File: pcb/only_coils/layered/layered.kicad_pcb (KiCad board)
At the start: 4 copper layers, 70 x 50 mm, 8 parts, among them J2 Conn_01x06_Pin, J4 Conn_01x03_Pin

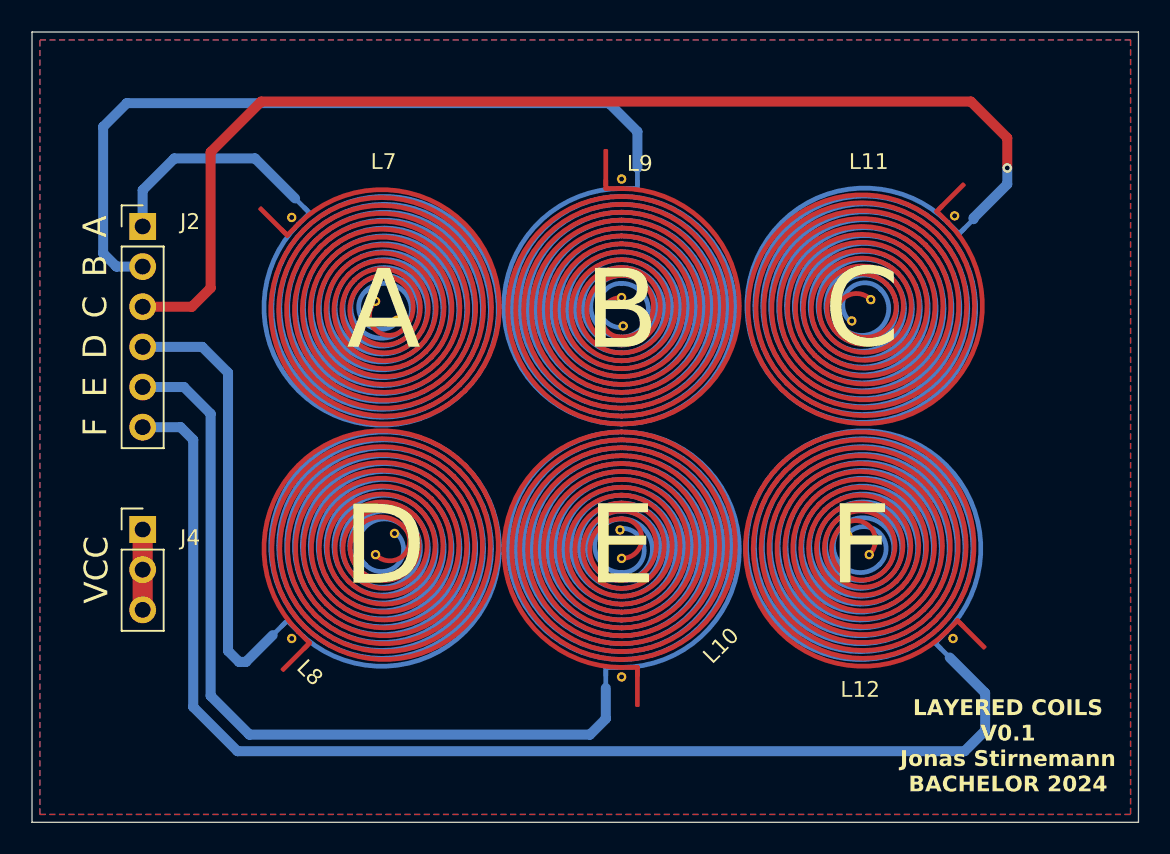
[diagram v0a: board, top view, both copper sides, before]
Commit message: Added small script for square coils
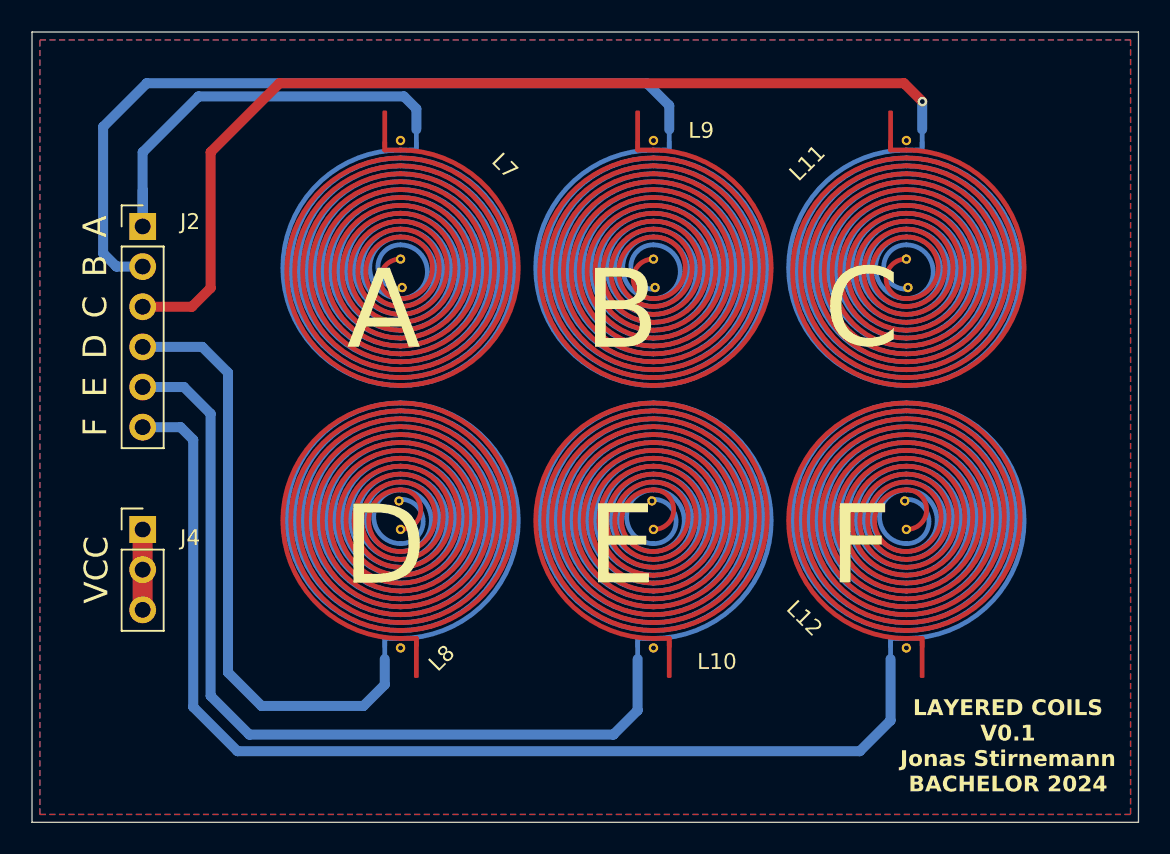
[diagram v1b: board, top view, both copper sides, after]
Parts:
- moved L11 3.66 mm to (122.0, 50.0), turned to 90 degrees
- moved L12 3.44 mm to (122.0, 65.5), turned to -90 degrees
- moved L9 3.16 mm to (106.0, 50.0)
- moved L10 2.73 mm to (106.0, 65.5)
- moved L7 2.64 mm to (90.0, 50.0), turned to 90 degrees
- moved L8 2.10 mm to (90.0, 65.5), turned to -90 degrees
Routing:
- net /A: track 13.8 -> 27.4 mm
- net /D: track 27.5 -> 38.0 mm
- net /C: track 72.1 -> 62.5 mm
- net /F: track 77.8 -> 70.4 mm
- net /E: track 51.2 -> 54.8 mm
- net /B: track 48.3 -> 49.9 mm
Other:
- board text added: "LAYERED MODULE - 4 layer coils - 12 turns / layer - 0.3 mm traces - 0.2 mm gap"
- board text removed: "LAYERED MODULE - 4 layer coils - 12 turns / layer - 0.3 mils traces - 0.2 mils gap"

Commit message: Added finished linear coils PCB
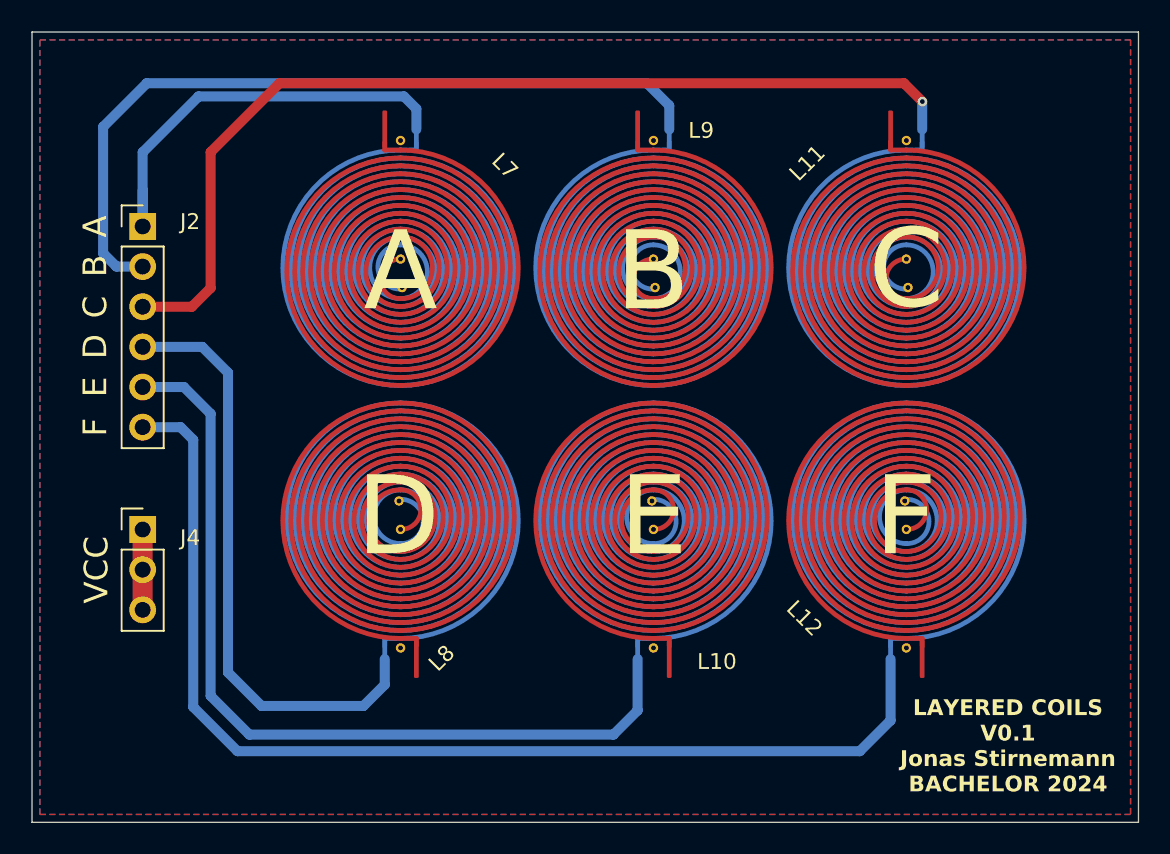
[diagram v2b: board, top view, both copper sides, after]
